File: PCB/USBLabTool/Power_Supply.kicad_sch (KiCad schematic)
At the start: 53 parts, among them J19 T_N5V, U10 Opamp_Quad, U11 DG403, U13 r1283, U14 ST1L05APU33R, U15 ST1L05APU33R, U16 LTC1983ES6-5#TRPBF, U9 Opamp_Quad

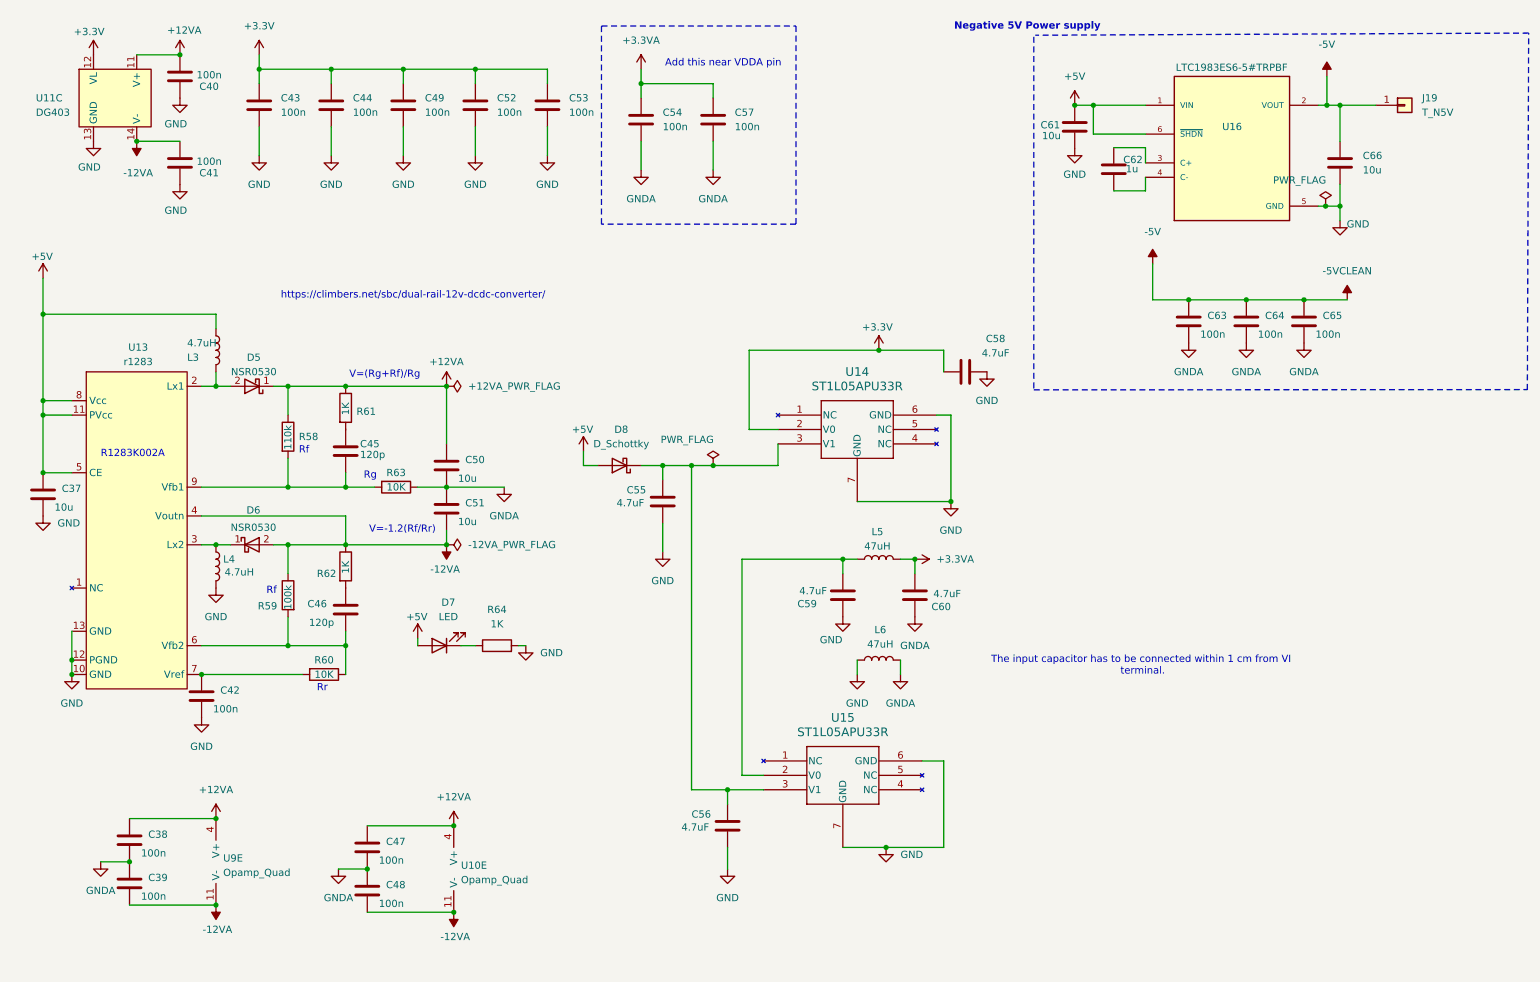
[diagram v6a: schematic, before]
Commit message: Resolved DRC/ERC errors in PCB and schematic
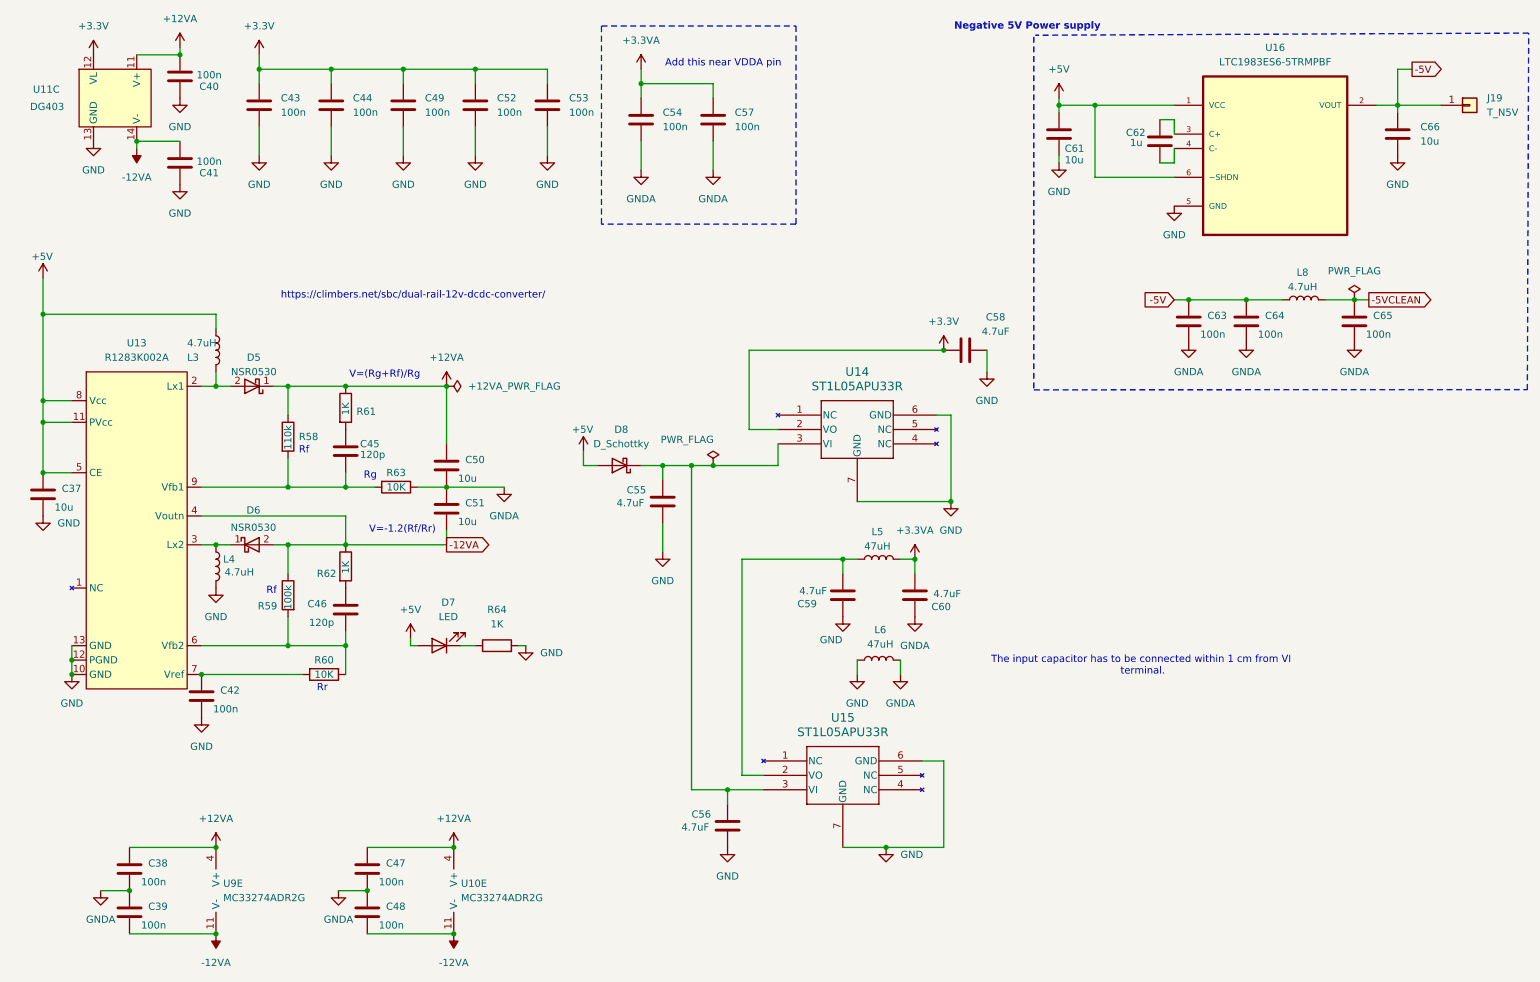
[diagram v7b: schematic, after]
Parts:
- removed U11: DG403, Package_SO:TSSOP-16-1EP_4.4x5mm_P0.65mm, symbol awg_lib:DG403
- removed U13: r1283, Package_DFN_QFN:ST_UFDFPN-12-1EP_3x3mm_P0.5mm_EP1.4x2.55mm, symbol awg_lib:r1283
- removed U16: LTC1983ES6-5#TRPBF, Package_TO_SOT_SMD:SOT-23-6_Handsoldering, symbol LTC1983ES6-5_TRPBF:LTC1983ES6-5#TRPBF
- added L8: 4.7uH, Inductor_SMD:L_0603_1608Metric_Pad1.05x0.95mm_HandSolder, symbol Device:L
- added U11: DG403, Package_SO:TSSOP-16_4.4x5mm_P0.65mm, symbol USBLabTool:DG403
- added U13: R1283K002A, Package_DFN_QFN:ST_UFDFPN-12-1EP_3x3mm_P0.5mm_EP1.4x2.55mm, symbol USBLabTool:r1283x
- added U16: LTC1983ES6-5TRMPBF, Package_TO_SOT_SMD:TSOT-23-6_HandSoldering, symbol USBLabTool:LTC1983ES6-5TRMPBF
- U10: value Opamp_Quad -> MC33274ADR2G
- U9: value Opamp_Quad -> MC33274ADR2G; BUY https://www.digikey.com/en/products/detail/onsemi/MC33274AD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 -> (none)
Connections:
- net +12VA: now also U11.11 (V+)
- net +3.3V: now also U11.12 (VL)
- net +5V: now also U13.11 (PVcc), U13.5 (CE), U13.8 (Vcc), U16.1 (VCC), U16.6 (~SHDN)
- net -12VA: now also U11.14 (V-), U13.4 (Voutn)
- net -5V: now also L8.1, U16.2 (VOUT); no longer C65.1
- net GND: now also U11.13 (GND), U13.10 (GND), U13.12 (PGND), U13.13 (GND), U16.5 (GND)
- net at C62.1: now also U16.3 (C+)
- net at C62.2: now also U16.4 (C-)
- net at C45.2, R58.2, R63.2: now also U13.9 (Vfb1)
- net at C46.2, R59.2, R60.1: now also U13.6 (Vfb2)
- net at D5.2 (A), L3.2: now also U13.2 (Lx1)
- net at D6.1 (K), L4.1: now also U13.3 (Lx2)
- net at C42.1, R60.2: now also U13.7 (Vref)
- new net -5VCLEAN: C65.1, L8.2
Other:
- note removed: "R1283K002A"
- moved on the sheet: C38, C39, C47, C48, C58, C61, C62, C65, C66, J19
